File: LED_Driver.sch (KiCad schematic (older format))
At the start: 6 parts, among them U5 AP5726

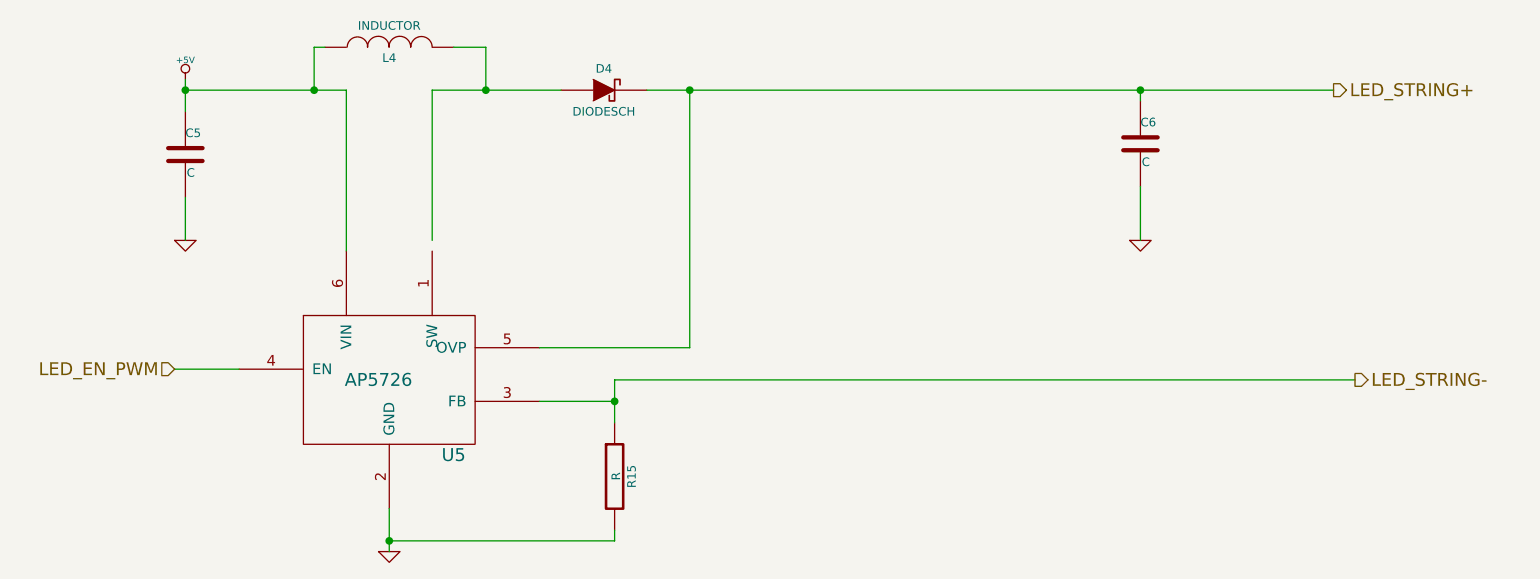
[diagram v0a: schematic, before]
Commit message: LED driver: assc/placement
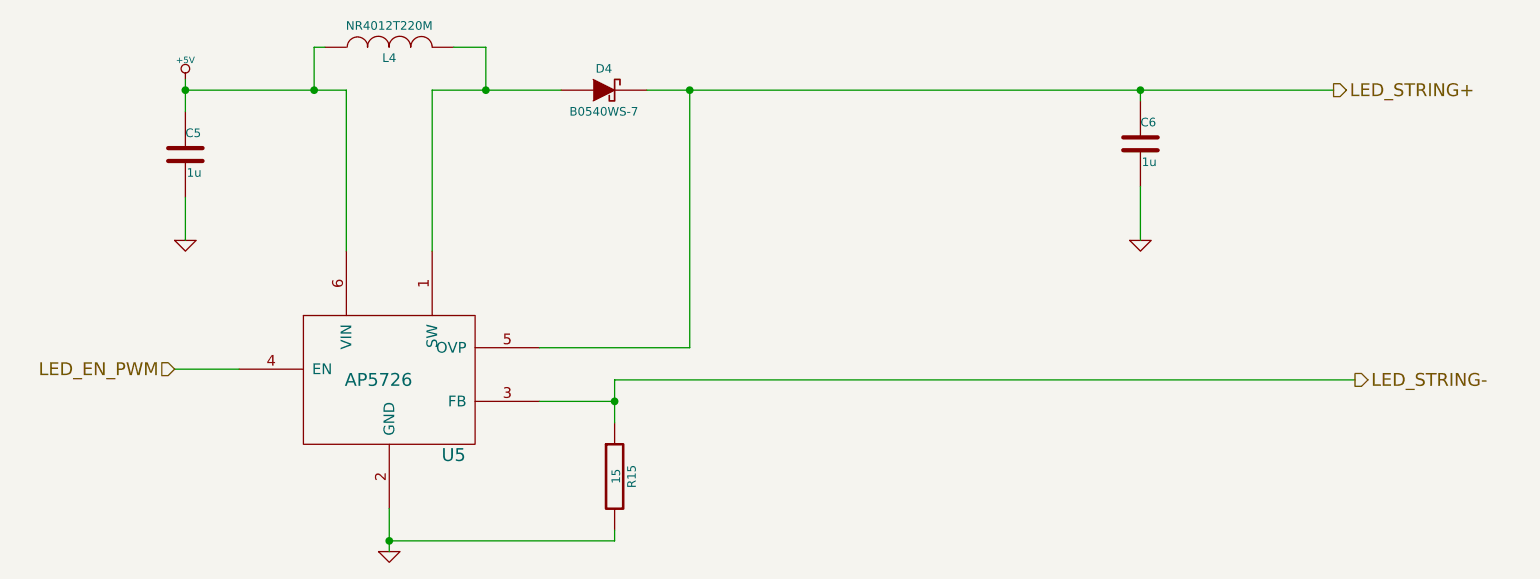
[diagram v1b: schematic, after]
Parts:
- C5, C6: value C -> 1u
- D4: value DIODESCH -> B0540WS-7
- L4: value INDUCTOR -> NR4012T220M
- R15: value R -> 15
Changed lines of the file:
@@
 Sheet 3 9
 Title ""
-Date "23 feb 2014"
+Date "24 feb 2014"
 Rev ""
 Comp ""
@@
 	2400 2700 2700 2700
 $Comp
-L +5V #PWR17
+L +5V #PWR015
 U 1 1 52F70E27
 P 2450 1350
-F 0 "#PWR17" H 2450 1440 20  0001 C CNN
+F 0 "#PWR015" H 2450 1440 20  0001 C CNN
 F 1 "+5V" H 2450 1440 30  0000 C CNN
 F 2 "" H 2450 1350 60  0000 C CNN
@@
 $EndComp
 $Comp
-L GND #PWR20
+L GND #PWR016
 U 1 1 52F70E36
 P 6900 2100
-F 0 "#PWR20" H 6900 2100 30  0001 C CNN
+F 0 "#PWR016" H 6900 2100 30  0001 C CNN
 F 1 "GND" H 6900 2030 30  0001 C CNN
 F 2 "" H 6900 2100 60  0000 C CNN
@@
 $EndComp
 $Comp
-L GND #PWR18
+L GND #PWR017
 U 1 1 52F70E4F
 P 2450 2100
-F 0 "#PWR18" H 2450 2100 30  0001 C CNN
+F 0 "#PWR017" H 2450 2100 30  0001 C CNN
 F 1 "GND" H 2450 2030 30  0001 C CNN
 F 2 "" H 2450 2100 60  0000 C CNN
@@
 P 2450 1700
 F 0 "C5" H 2450 1800 40  0000 L CNN
-F 1 "C" H 2456 1615 40  0000 L CNN
+F 1 "1u" H 2456 1615 40  0000 L CNN
 F 2 "~" H 2488 1550 30  0000 C CNN
 F 3 "~" H 2450 1700 60  0000 C CNN
@@
 P 6900 1650
 F 0 "C6" H 6900 1750 40  0000 L CNN
-F 1 "C" H 6906 1565 40  0000 L CNN
+F 1 "1u" H 6906 1565 40  0000 L CNN
 F 2 "~" H 6938 1500 30  0000 C CNN
 F 3 "~" H 6900 1650 60  0000 C CNN
@@
 P 3400 1200
 F 0 "L4" V 3350 1200 40  0000 C CNN
-F 1 "INDUCTOR" V 3500 1200 40  0000 C CNN
+F 1 "NR4012T220M" V 3500 1200 40  0000 C CNN
 F 2 "~" H 3400 1200 60  0000 C CNN
 F 3 "~" H 3400 1200 60  0000 C CNN
@@
 Connection ~ 3050 1400
 Wire Wire Line
-	3600 2100 3600 1400
+	3600 1400 3600 2150
 Wire Wire Line
 	3600 1400 4200 1400
@@
 P 4400 1400
 F 0 "D4" H 4400 1500 40  0000 C CNN
-F 1 "DIODESCH" H 4400 1300 40  0000 C CNN
+F 1 "B0540WS-7" H 4400 1300 40  0000 C CNN
 F 2 "~" H 4400 1400 60  0000 C CNN
 F 3 "~" H 4400 1400 60  0000 C CNN
@@
 P 4450 3200
 F 0 "R15" V 4530 3200 40  0000 C CNN
-F 1 "R" V 4457 3201 40  0000 C CNN
+F 1 "15" V 4457 3201 40  0000 C CNN
 F 2 "~" V 4380 3200 30  0000 C CNN
 F 3 "~" H 4450 3200 30  0000 C CNN
@@
 	4450 2750 4450 2950
 $Comp
-L GND #PWR19
+L GND #PWR018
 U 1 1 52F70F6C
 P 3400 3550
-F 0 "#PWR19" H 3400 3550 30  0001 C CNN
+F 0 "#PWR018" H 3400 3550 30  0001 C CNN
 F 1 "GND" H 3400 3480 30  0001 C CNN
 F 2 "" H 3400 3550 60  0000 C CNN
